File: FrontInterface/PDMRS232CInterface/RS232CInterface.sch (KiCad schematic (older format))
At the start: 31 parts, among them IC1 ADM3251EARWZ, J1 Screw_Terminal_01x02, J2 DB9_Female, J4 Conn_01x04, U1 MCP2561-E-SN, U2 MCP16301, U3 BluePill_STM32F103C

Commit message: PCB Update
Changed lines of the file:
@@
 EESchema Schematic File Version 4
-LIBS:RS232C Interface-cache
+LIBS:RS232CInterface-cache
 EELAYER 26 0
 EELAYER END
@@
 U 5DA86345
 F0 "PDM" 50
-F1 "file PDM.sch" 50
+F1 "filePDM.sch" 50
 F2 "CANH" I L 9650 1800 50
 F3 "CANL" I L 9650 2000 50

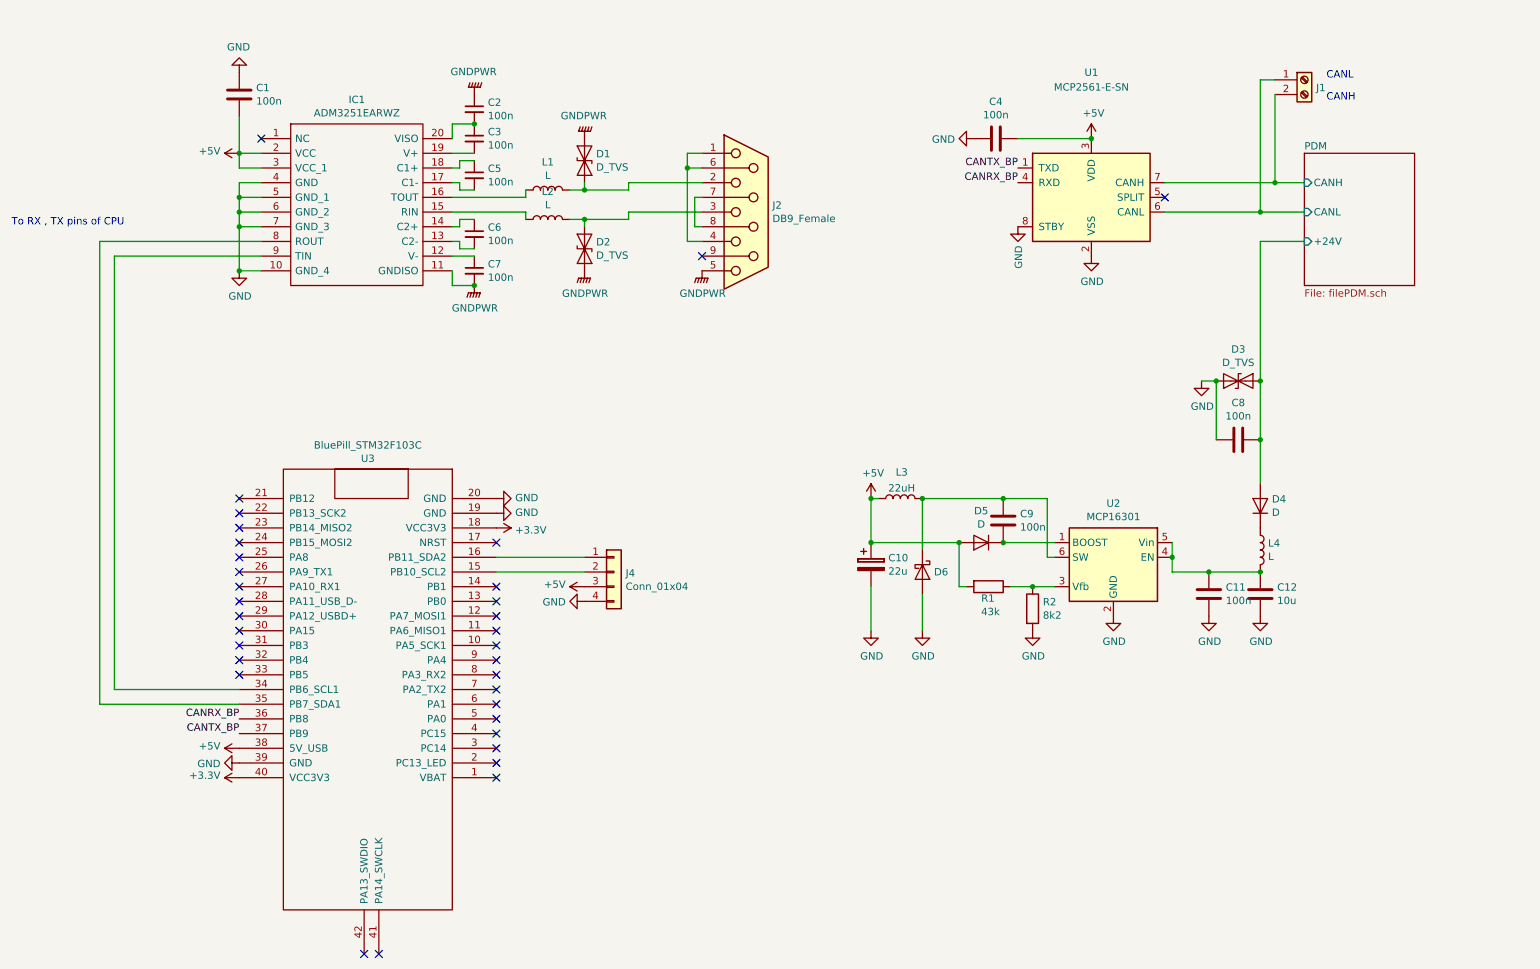
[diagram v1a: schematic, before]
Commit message: PCB updated, Lever Shifter added
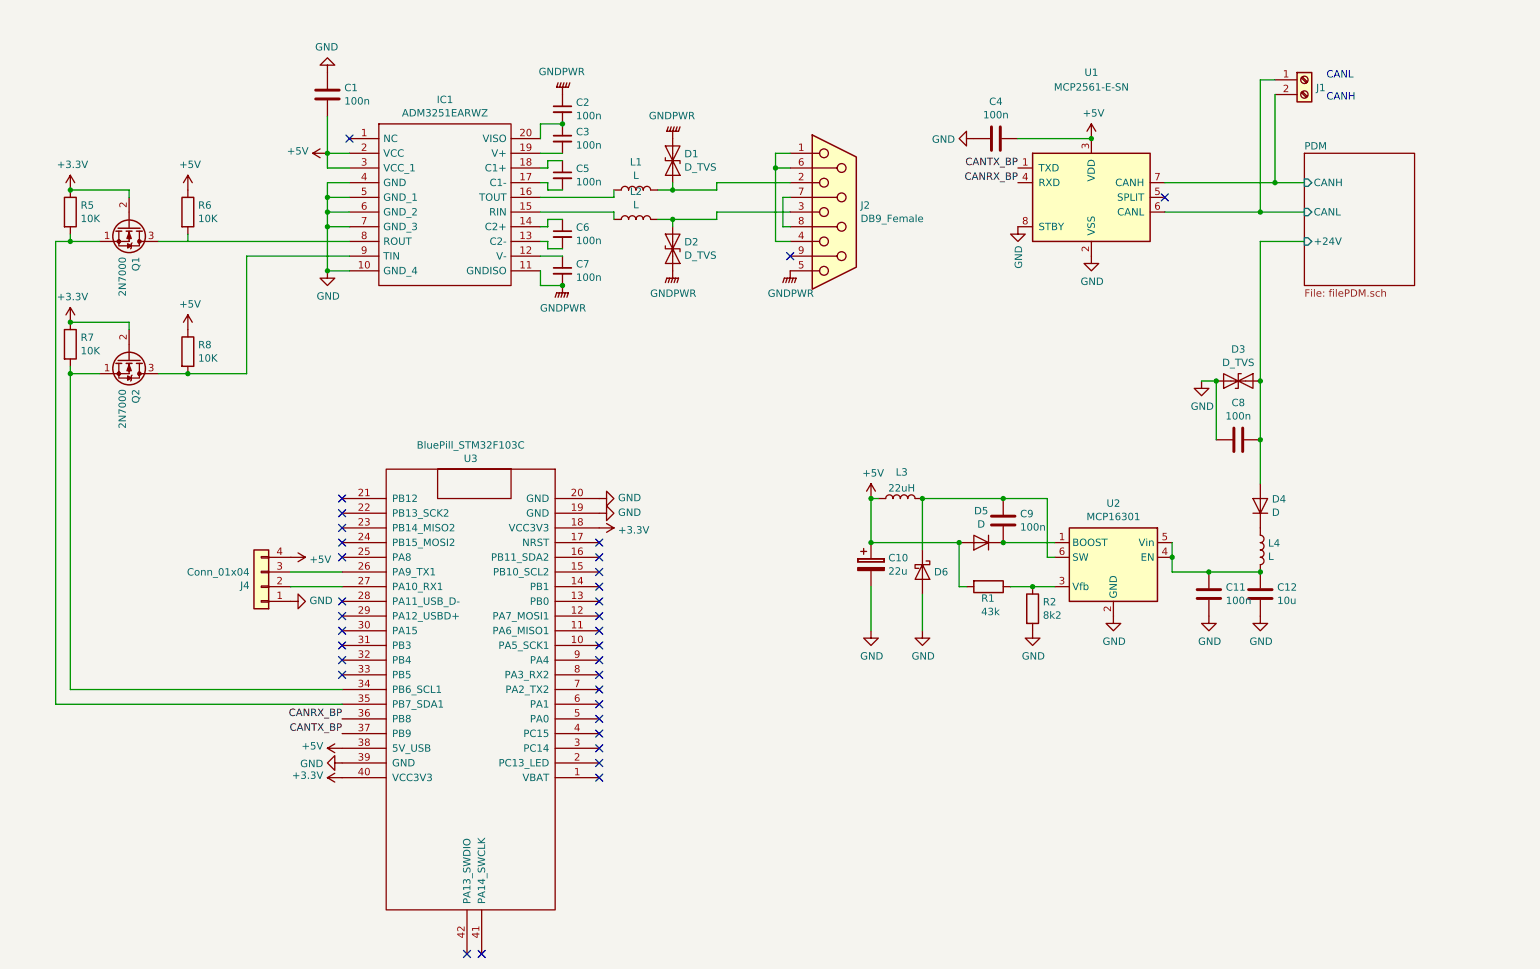
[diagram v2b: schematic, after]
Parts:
- added Q1, Q2: 2N7000, Package_TO_SOT_THT:TO-92_Inline, symbol Transistor_FET:2N7000
- added R5, R6, R7, R8: 10K, RS232C-Interface+PDM:RESistor0805, symbol Device:R
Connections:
- net +3V3: now also Q1.2 (G), Q2.2 (G), R5.1, R7.1
- net +5V: now also J4.4 (Pin_4), R6.1, R8.1; no longer J4.3 (Pin_3)
- net GND: now also J4.1 (Pin_1); no longer J4.4 (Pin_4)
- net at IC1.8 (ROUT): now also Q1.3 (D), R6.2; no longer U3.35 (PB7_SDA1)
- net at IC1.9 (TIN): now also Q2.3 (D), R8.2; no longer U3.34 (PB6_SCL1)
- net at U3.15 (PB10_SCL2): no longer J4.2 (Pin_2)
- net at U3.16 (PB11_SDA2): no longer J4.1 (Pin_1)
- net at U3.26 (PA9_TX1): now also J4.3 (Pin_3)
- net at U3.27 (PA10_RX1): now also J4.2 (Pin_2)
- new net: Q2.1 (S), R7.2, U3.34 (PB6_SCL1)
- new net: Q1.1 (S), R5.2, U3.35 (PB7_SDA1)
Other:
- note removed: "To RX , TX pins of CPU"
- moved on the sheet: C1, C2, C3, C5, C6, C7, D1, D2, IC1, J2, J4, L1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

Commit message: PCB updated
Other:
- moved on the sheet: C1, C10, C11, C12, C2, C3, C4, C5, C6, C7, C8, C9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

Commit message: Zones and routes updated
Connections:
- net GNDPWR renamed GNDS
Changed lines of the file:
@@
 	4350 6000 4500 6000
-$Comp
-L power:GNDPWR #PWR0118
-U 1 1 5D78D5E7
-P 4500 6000
-F 0 "#PWR0118" H 4500 5800 50  0001 C CNN
-F 1 "GNDPWR" H 4504 5846 50  0000 C CNN
-F 2 "" H 4500 5950 50  0001 C CNN
-F 3 "" H 4500 5950 50  0001 C CNN
-	1    4500 6000
-	1    0    0    -1
-$EndComp
-Connection ~ 4500 6000
 $Comp
 L Device:C_Small C6
@@
 Connection ~ 4500 4900
 $Comp
-L power:GNDPWR #PWR0119
-U 1 1 5D796FC3
-P 4500 4700
-F 0 "#PWR0119" H 4500 4500 50  0001 C CNN
-F 1 "GNDPWR" H 4505 4545 50  0000 C CNN
-F 2 "" H 4500 4650 50  0001 C CNN
-F 3 "" H 4500 4650 50  0001 C CNN
-	1    4500 4700
-	-1   0    0    1
-$EndComp
-$Comp
 L Device:L L1
 U 1 1 5D799229
@@
 	5250 5350 5250 5300
 $Comp
-L power:GNDPWR #PWR0120
-U 1 1 5D7A80D6
-P 5250 5900
-F 0 "#PWR0120" H 5250 5700 50  0001 C CNN
-F 1 "GNDPWR" H 5254 5746 50  0000 C CNN
-F 2 "" H 5250 5850 50  0001 C CNN
-F 3 "" H 5250 5850 50  0001 C CNN
-	1    5250 5900
-	1    0    0    -1
-$EndComp
-$Comp
-L power:GNDPWR #PWR0121
-U 1 1 5D7A81E3
-P 5250 5000
-F 0 "#PWR0121" H 5250 4800 50  0001 C CNN
-F 1 "GNDPWR" H 5255 4845 50  0000 C CNN
-F 2 "" H 5250 4950 50  0001 C CNN
-F 3 "" H 5250 4950 50  0001 C CNN
-	1    5250 5000
-	-1   0    0    1
-$EndComp
-$Comp
 L Connector:DB9_Female J2
 U 1 1 5D7B6CE3
@@
 F 3 "https://de.rs-online.com/web/p/sub-d-steckverbinder-leiterplatte/7718329/" H 6350 5500 50  0001 C CNN
 	1    6350 5500
-	1    0    0    -1
-$EndComp
-$Comp
-L power:GNDPWR #PWR0122
-U 1 1 5D7B6FA7
-P 6050 5900
-F 0 "#PWR0122" H 6050 5700 50  0001 C CNN
-F 1 "GNDPWR" H 6054 5746 50  0000 C CNN
-F 2 "" H 6050 5850 50  0001 C CNN
-F 3 "" H 6050 5850 50  0001 C CNN
-	1    6050 5900
 	1    0    0    -1
 $EndComp
@@
 	950  2350 2900 2350
 Connection ~ 1150 6600
+$Comp
+L power:GNDS #PWR0118
+U 1 1 5DD36D17
+P 5250 5900
+F 0 "#PWR0118" H 5250 5650 50  0001 C CNN
+F 1 "GNDS" H 5255 5727 50  0000 C CNN
+F 2 "" H 5250 5900 50  0001 C CNN
+F 3 "" H 5250 5900 50  0001 C CNN
+	1    5250 5900
+	1    0    0    -1
+$EndComp
+$Comp
+L power:GNDS #PWR0119
+U 1 1 5DD3E611
+P 4500 6000
+F 0 "#PWR0119" H 4500 5750 50  0001 C CNN
+F 1 "GNDS" H 4505 5827 50  0000 C CNN
+F 2 "" H 4500 6000 50  0001 C CNN
+F 3 "" H 4500 6000 50  0001 C CNN
+	1    4500 6000
+	1    0    0    -1
+$EndComp
+$Comp
+L power:GNDS #PWR0120
+U 1 1 5DD422E6
+P 6050 5900
+F 0 "#PWR0120" H 6050 5650 50  0001 C CNN
+F 1 "GNDS" H 6055 5727 50  0000 C CNN
+F 2 "" H 6050 5900 50  0001 C CNN
+F 3 "" H 6050 5900 50  0001 C CNN
+	1    6050 5900
+	1    0    0    -1
+$EndComp
+$Comp
+L power:GNDS #PWR0121
+U 1 1 5DD46309
+P 5250 5000
+F 0 "#PWR0121" H 5250 4750 50  0001 C CNN
+F 1 "GNDS" H 5255 4827 50  0000 C CNN
+F 2 "" H 5250 5000 50  0001 C CNN
+F 3 "" H 5250 5000 50  0001 C CNN
+	1    5250 5000
+	-1   0    0    1
+$EndComp
+$Comp
+L power:GNDS #PWR0122
+U 1 1 5DD58CEF
+P 4500 4700
+F 0 "#PWR0122" H 4500 4450 50  0001 C CNN
+F 1 "GNDS" H 4505 4527 50  0000 C CNN
+F 2 "" H 4500 4700 50  0001 C CNN
+F 3 "" H 4500 4700 50  0001 C CNN
+	1    4500 4700
+	-1   0    0    1
+$EndComp
 $EndSCHEMATC
